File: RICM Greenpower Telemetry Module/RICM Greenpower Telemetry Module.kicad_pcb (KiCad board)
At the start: 2 copper layers, 62.5 x 119 mm, 45 parts, among them J1 Jack-DC, J10 Conn_01x02_Female, J11 Conn_01x02_Female, J2 Conn_01x05_Female, J3 Conn_02x04_Counter_Clockwise, J4 Conn_01x03_Female, J5 Conn_01x03_Female, J6 Conn_01x02_Female, J7 Conn_01x02_Female, J8 Conn_01x02_Female, J9 Conn_01x04_Female, U1 XL2001E1, U2 Pico, U3 MPU_6050_module, U4 Adafruit_MicroSD_SPI_SDIO, U5 ADS7830

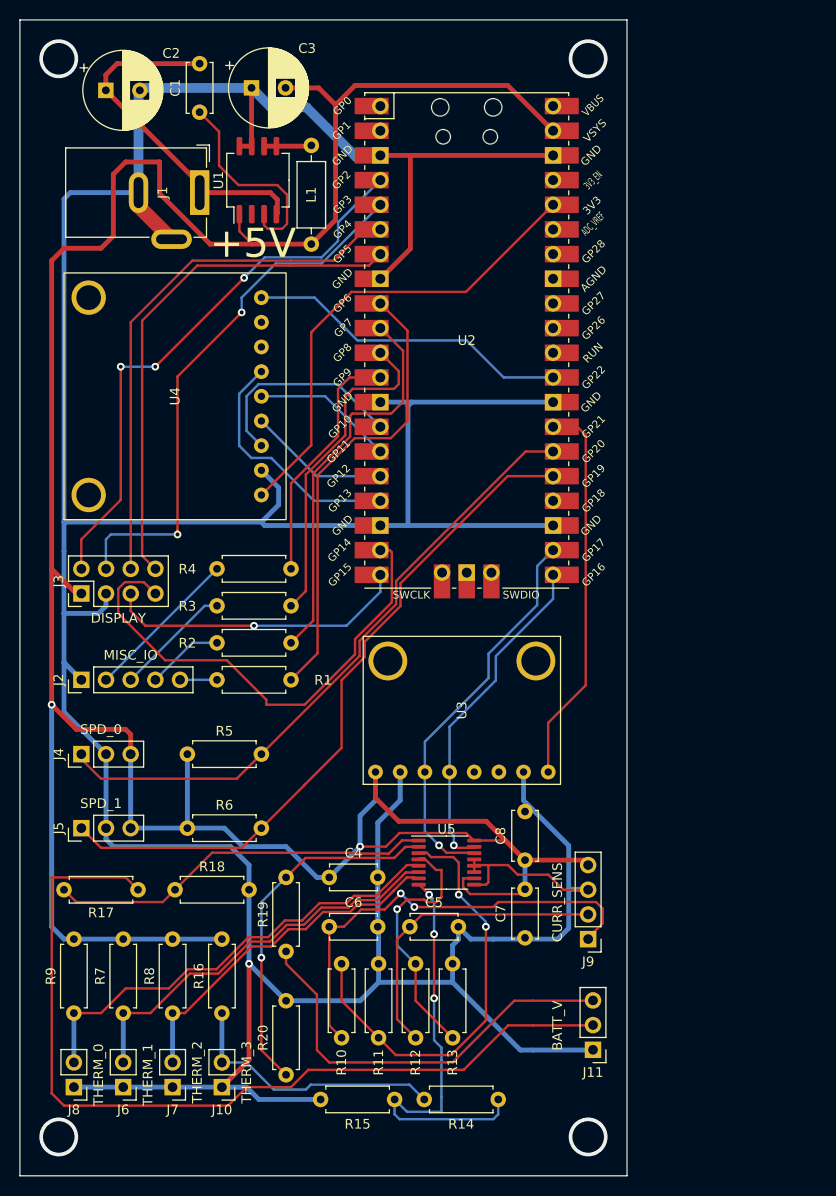
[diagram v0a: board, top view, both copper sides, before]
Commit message: Added pullups for i2c
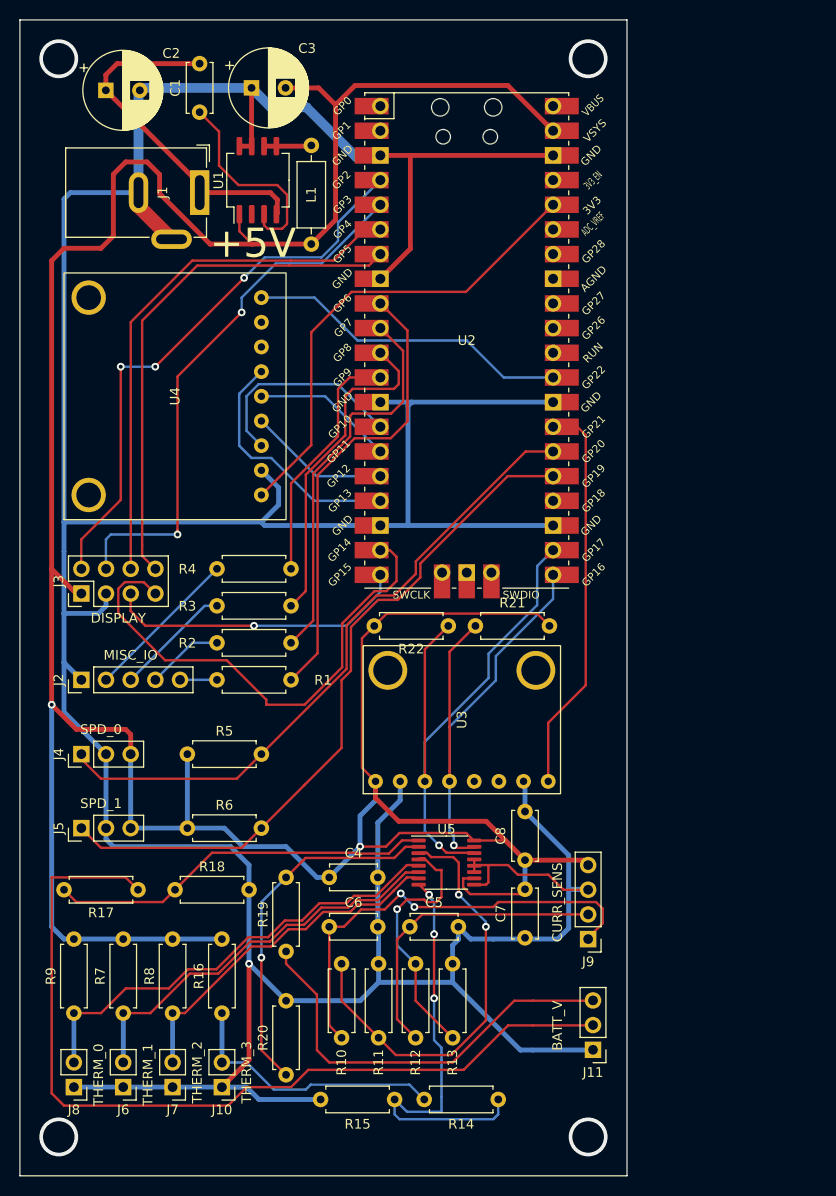
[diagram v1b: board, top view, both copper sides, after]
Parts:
- added R21: 4.7k, Resistor_THT:R_Axial_DIN0207_L6.3mm_D2.5mm_P7.62mm_Horizontal, F.Cu at (56.9, 72.4)
- added R22: 4.7k, Resistor_THT:R_Axial_DIN0207_L6.3mm_D2.5mm_P7.62mm_Horizontal, F.Cu at (54.1, 72.4)
- moved U3 0.96 mm to (55.5, 82.0)
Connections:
- J1 pad 3: GND -> (no net)
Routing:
- net +5V: track 298.1 -> 331.5 mm
- net I2C_SDA: track 34.8 -> 51.9 mm
- net I2C_SCL: track 40.3 -> 57.3 mm
- net GND: track 440.5 -> 438.4 mm
- net SPD_1: track 71.6 -> 72.8 mm
- net I2C0_SDA: track 51.2 -> 52.3 mm
- net SPD_0: track 66.2 -> 67.3 mm
- net ACC_INT: track 37.3 -> 38.3 mm

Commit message: rearranged board
Switched to sdm resistors and capacitors. Added a 3v3 regulated supply. Various other revisions.
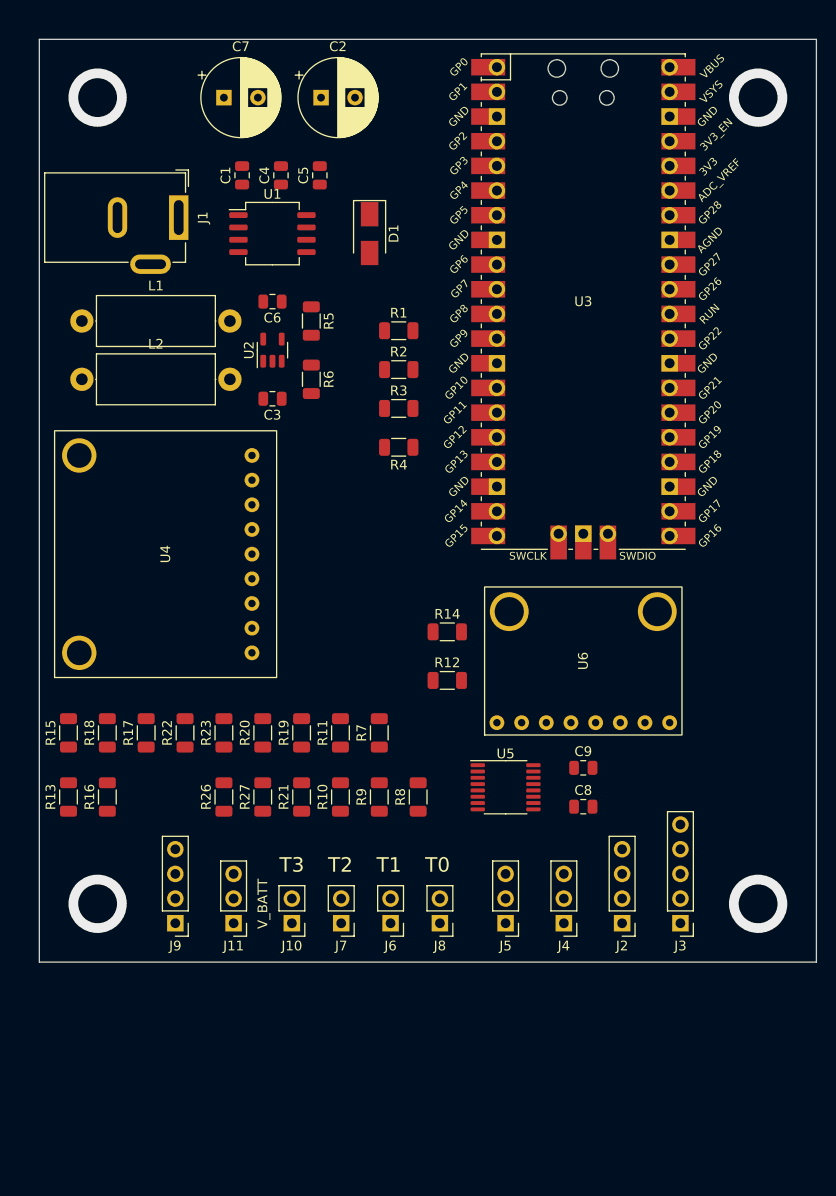
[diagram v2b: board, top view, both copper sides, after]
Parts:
- added C9: 10uf, Capacitor_SMD:C_0805_2012Metric, F.Cu at (68.0, 87.0)
- added D1: D_Schottky, Diode_SMD:D_SMA, F.Cu at (46.0, 32.0)
- added L2: 47uh, Inductor_THT:L_Axial_L12.0mm_D5.0mm_P15.24mm_Horizontal_Fastron_MISC, F.Cu at (16.4, 47.0)
- added R23: 10k, Resistor_SMD:R_1206_3216Metric, F.Cu at (31.0, 83.4)
- added R26: 68k, Resistor_SMD:R_1206_3216Metric, F.Cu at (31.0, 90.0)
- added R27: 10k, Resistor_SMD:R_1206_3216Metric, F.Cu at (35.0, 90.0)
- added U6: MPU_6050_module, Module:MPU_6050_module, F.Cu at (68.0, 76.0)
- C1: value C -> 10uf; footprint Capacitor_THT:C_Disc_D5.0mm_W2.5mm_P5.00mm -> Capacitor_SMD:C_0805_2012Metric
- C2: value C -> 47uf
- C3: value C -> 10uf; footprint Capacitor_THT:CP_Radial_D8.0mm_P3.50mm -> Capacitor_SMD:C_0805_2012Metric
- C4, C6: value 47n -> 10uf; footprint Capacitor_THT:C_Disc_D4.7mm_W2.5mm_P5.00mm -> Capacitor_SMD:C_0805_2012Metric
- C5: value 4.7n -> 10uf; footprint Capacitor_THT:C_Disc_D4.7mm_W2.5mm_P5.00mm -> Capacitor_SMD:C_0805_2012Metric
- C7: value C -> 100uf; footprint Capacitor_THT:C_Disc_D5.0mm_W2.5mm_P5.00mm -> Capacitor_THT:CP_Radial_D8.0mm_P3.50mm
- C8: value C -> 0.1uf; footprint Capacitor_THT:C_Disc_D5.0mm_W2.5mm_P5.00mm -> Capacitor_SMD:C_0805_2012Metric
- J2: value Conn_01x05_Female -> Conn_01x04_Female; footprint Connector_PinHeader_2.54mm:PinHeader_1x05_P2.54mm_Vertical -> Connector_PinHeader_2.54mm:PinHeader_1x04_P2.54mm_Vertical
- J3: value Conn_02x04_Counter_Clockwise -> Conn_01x05_Female; footprint Connector_PinHeader_2.54mm:PinHeader_2x04_P2.54mm_Vertical -> Connector_PinHeader_2.54mm:PinHeader_1x05_P2.54mm_Vertical
- L1: value L -> 47uh; footprint Inductor_THT:L_Axial_L6.6mm_D2.7mm_P10.16mm_Horizontal_Vishay_IM-2 -> Inductor_THT:L_Axial_L12.0mm_D5.0mm_P15.24mm_Horizontal_Fastron_MISC
- R1, R10, R11, R13, R15, R16, R18, R2, R20, R3, R4, R6, R7, R8, R9: footprint Resistor_THT:R_Axial_DIN0207_L6.3mm_D2.5mm_P7.62mm_Horizontal -> Resistor_SMD:R_1206_3216Metric
- R12, R14: value 10k -> 4.7k; footprint Resistor_THT:R_Axial_DIN0207_L6.3mm_D2.5mm_P7.62mm_Horizontal -> Resistor_SMD:R_1206_3216Metric
- R17: value 30k -> 10k; footprint Resistor_THT:R_Axial_DIN0207_L6.3mm_D2.5mm_P7.62mm_Horizontal -> Resistor_SMD:R_1206_3216Metric
- R19: value 68k -> 10k; footprint Resistor_THT:R_Axial_DIN0207_L6.3mm_D2.5mm_P7.62mm_Horizontal -> Resistor_SMD:R_1206_3216Metric
- R21: value 4.7k -> 10k; footprint Resistor_THT:R_Axial_DIN0207_L6.3mm_D2.5mm_P7.62mm_Horizontal -> Resistor_SMD:R_1206_3216Metric
- R22: value 4.7k -> 30k; footprint Resistor_THT:R_Axial_DIN0207_L6.3mm_D2.5mm_P7.62mm_Horizontal -> Resistor_SMD:R_1206_3216Metric
- R5: value 10k -> 47k; footprint Resistor_THT:R_Axial_DIN0207_L6.3mm_D2.5mm_P7.62mm_Horizontal -> Resistor_SMD:R_1206_3216Metric
- U2: value Pico -> MT92165; footprint Module:RPi_Pico_SMD_TH -> Package_TO_SOT_SMD:SOT-23-5
- U3: value MPU_6050_module -> Pico; footprint Module:MPU_6050_module -> Module:RPi_Pico_SMD_TH
- moved C7 87.2 mm to (31.0, 18.0), turned to 0 degrees
- moved C5 77.9 mm to (40.9, 26.0), turned to 90 degrees
- moved C4 72.5 mm to (36.9, 26.0), turned to 90 degrees
- moved J3 70.4 mm to (78.0, 103.0), turned to 180 degrees
- moved C6 64.6 mm to (36.0, 39.0), turned to 180 degrees
- moved J2 61.1 mm to (72.0, 103.0), turned to 180 degrees
- moved J4 52.6 mm to (66.0, 103.0), turned to 180 degrees
- moved R14 48.2 mm to (54.0, 73.0)
- moved R6 47.9 mm to (40.0, 47.0), turned to -90 degrees
- moved R13 46.7 mm to (15.0, 90.0)
- moved R5 46.4 mm to (40.0, 41.0), turned to -90 degrees
- moved R15 45.8 mm to (15.0, 83.4), turned to 90 degrees
- moved U3 44.8 mm to (68.0, 39.0), turned to 0 degrees
- moved J5 44.8 mm to (60.0, 103.0), turned to 180 degrees
- moved J9 42.5 mm to (26.0, 103.0)
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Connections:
- C3 pad 1: GND -> +5V
- C3 pad 2: +5V -> Net-(C3-Pad2)
- C4 pad 1: +5V -> Net-(C1-Pad2)
- C5 pad 1: Net-(C5-Pad1) -> +5V
- C6 pad 1: Net-(C6-Pad1) -> +3V3
- C8 pad 1: +5V -> Net-(C8-Pad1)
- J2 pad 1: GND -> +3V3
- J2 pad 2: Net-(J2-Pad2) -> GND
- J2 pad 3: Net-(J2-Pad3) -> I2C0_SCL
- J2 pad 4: Net-(J2-Pad4) -> I2C0_SDA
- J3 pad 1: +5V -> GND
- J3 pad 2: GND -> Net-(J3-Pad2)
- J3 pad 3: I2C0_SCL -> Net-(J3-Pad3)
- J3 pad 4: I2C0_SDA -> Net-(J3-Pad4)
- J4 pad 3: +5V -> +3V3
- J5 pad 3: +5V -> +3V3
- J9 pad 1: Net-(C6-Pad1) -> +5V
- J9 pad 2: Net-(C5-Pad1) -> GND
- J9 pad 3: GND -> Net-(J9-Pad3)
- J9 pad 4: +5V -> Net-(J9-Pad4)
- R1 pad 1: Net-(J2-Pad5) -> Net-(J3-Pad5)
- R10 pad 1: Net-(C6-Pad1) -> THERM_2
- R10 pad 2: Net-(R10-Pad2) -> +3V3
- R11 pad 1: Net-(R10-Pad2) -> THERM_0
- R11 pad 2: GND -> +3V3
- R12 pad 1: Net-(C5-Pad1) -> I2C_SDA
- R12 pad 2: Net-(R12-Pad2) -> +3V3
- R13 pad 1: Net-(R12-Pad2) -> GND
- R13 pad 2: GND -> Net-(J9-Pad3)
- R14 pad 1: Net-(J10-Pad2) -> I2C_SCL
- R14 pad 2: THERM_3 -> +3V3
- R15 pad 1: GND -> Net-(J9-Pad3)
- R15 pad 2: THERM_3 -> Net-(R15-Pad2)
- R16 pad 1: Net-(J10-Pad2) -> Net-(R15-Pad2)
- R16 pad 2: +5V -> GND
- R17 pad 1: Net-(J11-Pad2) -> Net-(J9-Pad4)
- R19 pad 1: Net-(J11-Pad3) -> Net-(J10-Pad2)
- R19 pad 2: Net-(R19-Pad2) -> THERM_3
- R2 pad 1: Net-(J2-Pad4) -> Net-(J3-Pad4)
- R20 pad 1: Net-(R19-Pad2) -> GND
- R20 pad 2: GND -> THERM_3
- R21 pad 1: I2C_SDA -> Net-(J10-Pad2)
- R21 pad 2: +5V -> +3V3
- R22 pad 1: I2C_SCL -> Net-(J11-Pad2)
- R22 pad 2: +5V -> Net-(R22-Pad2)
- R3 pad 1: Net-(J2-Pad3) -> Net-(J3-Pad3)
- R4 pad 1: Net-(J2-Pad2) -> Net-(J3-Pad2)
- R5 pad 1: +5V -> +3V3
- R5 pad 2: SPD_0 -> Net-(R5-Pad2)
- R6 pad 1: +5V -> GND
- R6 pad 2: SPD_1 -> Net-(R5-Pad2)
- R7 pad 1: THERM_1 -> +3V3
- R7 pad 2: +5V -> SPD_0
- R8 pad 1: THERM_2 -> +3V3
- R8 pad 2: +5V -> SPD_1
- R9 pad 1: THERM_0 -> THERM_1
- R9 pad 2: +5V -> +3V3
- U2 pad 1: unconnected-(U2-Pad1) -> +5V
- U2 pad 2: unconnected-(U2-Pad2) -> GND
- U2 pad 3: GND -> Net-(C3-Pad2)
- U2 pad 4: Net-(J3-Pad8) -> Net-(L2-Pad1)
- U2 pad 5: Net-(J3-Pad7) -> Net-(R5-Pad2)
- U3 pad 1: +5V -> unconnected-(U3-Pad1)
- U3 pad 2: GND -> unconnected-(U3-Pad2)
- U3 pad 3: I2C_SCL -> GND
- U3 pad 4: I2C_SDA -> unconnected-(U3-Pad4)
- U3 pad 7: GND -> unconnected-(U3-Pad7)
- U3 pad 8: ACC_INT -> GND
- U5 pad 1: Net-(R17-Pad2) -> Net-(R22-Pad2)
- U5 pad 10: +5V -> Net-(C8-Pad1)
- U5 pad 16: +5V -> +3V3
- U5 pad 2: Net-(R19-Pad2) -> Net-(R26-Pad2)
- U5 pad 3: Net-(R10-Pad2) -> Net-(R15-Pad2)
- U5 pad 4: Net-(R12-Pad2) -> Net-(R17-Pad2)
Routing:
- net GND: track 438.4 -> 0.00 mm, vias 1 -> 0
- net +5V: track 331.5 -> 0.00 mm, vias 2 -> 0
- net Net-(J11-Pad2): track 91.3 -> 0.00 mm
- net SPD_1: track 72.8 -> 0.00 mm
- net SPD_0: track 67.3 -> 0.00 mm
- net Net-(J3-Pad8): track 58.3 -> 0.00 mm, vias 3 -> 0
- net I2C_SCL: track 57.3 -> 0.00 mm, vias 1 -> 0
- net Net-(J3-Pad7): track 56.0 -> 0.00 mm, vias 2 -> 0
- net Net-(J3-Pad6): track 54.8 -> 0.00 mm
- net Net-(J3-Pad5): track 53.5 -> 0.00 mm
- net I2C0_SDA: track 52.3 -> 0.00 mm
- net I2C_SDA: track 51.9 -> 0.00 mm, vias 1 -> 0
- net +3V3: track 49.2 -> 0.00 mm
- net Net-(R1-Pad2): track 47.1 -> 0.00 mm
- net THERM_0: track 47.0 -> 0.00 mm
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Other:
- board size 62.5 x 119 mm -> 80 x 95 mm
- board text added: "T0"
- board text added: "T1"
- board text added: "T2"
- board text added: "T3"
- board text added: "V_BATT"
- board text removed: "+5V"
- board text removed: "BATT_V"
- board text removed: "CURR_SENS"
- board text removed: "DISPLAY"
- board text removed: "MISC_IO"
- board text removed: "SPD_0"
- board text removed: "SPD_1"
- board text removed: "THERM_0"
- board text removed: "THERM_1"
- board text removed: "THERM_2"
- board text removed: "THERM_3"

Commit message: Moving to laptop
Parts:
- added R5: 10k, Resistor_SMD:R_1206_3216Metric, F.Cu at (86.5, 44.0)
- added R6: 10k, Resistor_SMD:R_1206_3216Metric, F.Cu at (86.5, 49.0)
- R1, R2: value 10k -> 4.7k
- moved R3 40.7 mm to (86.5, 34.0)
- moved R4 40.4 mm to (86.5, 39.0), turned to 0 degrees
- moved C2 25.8 mm to (18.0, 29.7), turned to 90 degrees
- moved R2 20.1 mm to (51.0, 66.0), turned to 180 degrees
- moved R1 19.1 mm to (51.0, 61.0), turned to 180 degrees
- moved J1 17.6 mm to (43.6, 27.4), turned to 180 degrees
- moved C1 8.12 mm to (25.0, 24.0)
- moved C4 8.12 mm to (29.0, 24.0)
- moved C5 8.12 mm to (33.0, 24.0)
- moved U1 6.00 mm to (30.0, 32.0)
- moved C7 3.07 mm to (28.0, 18.7), turned to 90 degrees
- moved D1 2.83 mm to (44.0, 34.0), turned to 0 degrees
- moved L1 1.38 mm to (15.0, 41.0)
- moved L2 1.38 mm to (15.0, 47.0)
- moved R7 1.00 mm to (41.0, 41.0)
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- renumbered R8 to R10, R9 to R11, R10 to R12, R11 to R13, R12 to R14, R13 to R15, R14 to R16, R15 to R17, R16 to R18, R17 to R19, R18 to R20, R19 to R21, R20 to R22, R21 to R23, R22 to R24, R23 to R25, R5 to R7, R6 to R8, R7 to R9
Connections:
- D1 pad 1: GND -> Net-(L1-Pad1)
- D1 pad 2: Net-(D1-Pad2) -> GND
- L1 pad 1: Net-(D1-Pad2) -> Net-(L1-Pad1)
- R1 pad 1: Net-(J3-Pad5) -> I2C0_SDA
- R1 pad 2: Net-(R1-Pad2) -> +3V3
- R2 pad 1: Net-(J3-Pad4) -> I2C0_SCL
- R2 pad 2: Net-(R2-Pad2) -> +3V3
- R3 pad 1: Net-(J3-Pad3) -> Net-(R3-Pad1)
- R3 pad 2: Net-(R3-Pad2) -> Net-(J3-Pad5)
- R4 pad 1: Net-(J3-Pad2) -> Net-(R4-Pad1)
- R4 pad 2: Net-(R4-Pad2) -> Net-(J3-Pad4)
- U1 pad 5: Net-(D1-Pad2) -> Net-(L1-Pad1)
- U1 pad 6: Net-(D1-Pad2) -> Net-(L1-Pad1)
- U3 pad 10: Net-(R2-Pad2) -> Net-(R4-Pad1)
- U3 pad 11: Net-(R3-Pad2) -> Net-(R5-Pad1)
- U3 pad 12: Net-(R4-Pad2) -> Net-(R6-Pad1)
- U3 pad 9: Net-(R1-Pad2) -> Net-(R3-Pad1)
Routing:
- net GND: track 0.00 -> 435.0 mm, vias 0 -> 5
- net +5V: track 0.00 -> 175.9 mm, vias 0 -> 3
- net +3V3: track 0.00 -> 174.2 mm, vias 0 -> 7
- net SPD_0: track 0.00 -> 79.8 mm, vias 0 -> 2
- net SPD_1: track 0.00 -> 74.9 mm, vias 0 -> 5
- net Net-(J3-Pad5): track 0.00 -> 63.8 mm, vias 0 -> 2
- net Net-(J3-Pad4): track 0.00 -> 61.3 mm, vias 0 -> 2
- net Net-(J3-Pad3): track 0.00 -> 58.0 mm
- net I2C0_SDA: track 0.00 -> 57.7 mm, vias 0 -> 3
- net SD_DET: track 0.00 -> 57.7 mm, vias 0 -> 2
- net I2C0_SCL: track 0.00 -> 56.9 mm, vias 0 -> 2
- net Net-(J3-Pad2): track 0.00 -> 55.6 mm
- net I2C_SCL: track 0.00 -> 55.0 mm, vias 0 -> 2
- net Net-(C1-Pad2): track 0.00 -> 53.6 mm, vias 0 -> 1
- net I2C_SDA: track 0.00 -> 52.9 mm, vias 0 -> 1
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
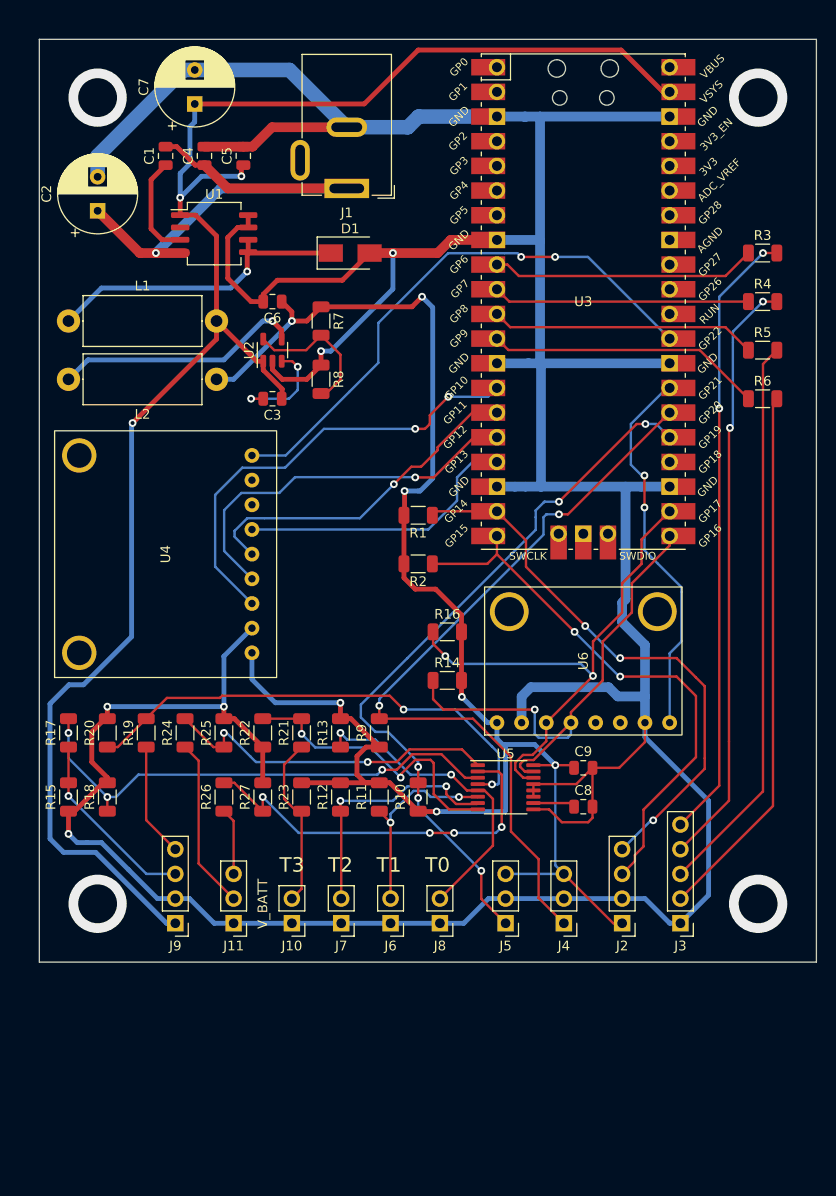
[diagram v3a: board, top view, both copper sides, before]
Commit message: fixed errors discovered in v1 board
Connected vref on the ADS7830 to 3v3.
Corrected swapped pins on MT9216.
Added silkscreens and readjusted connector numbering.
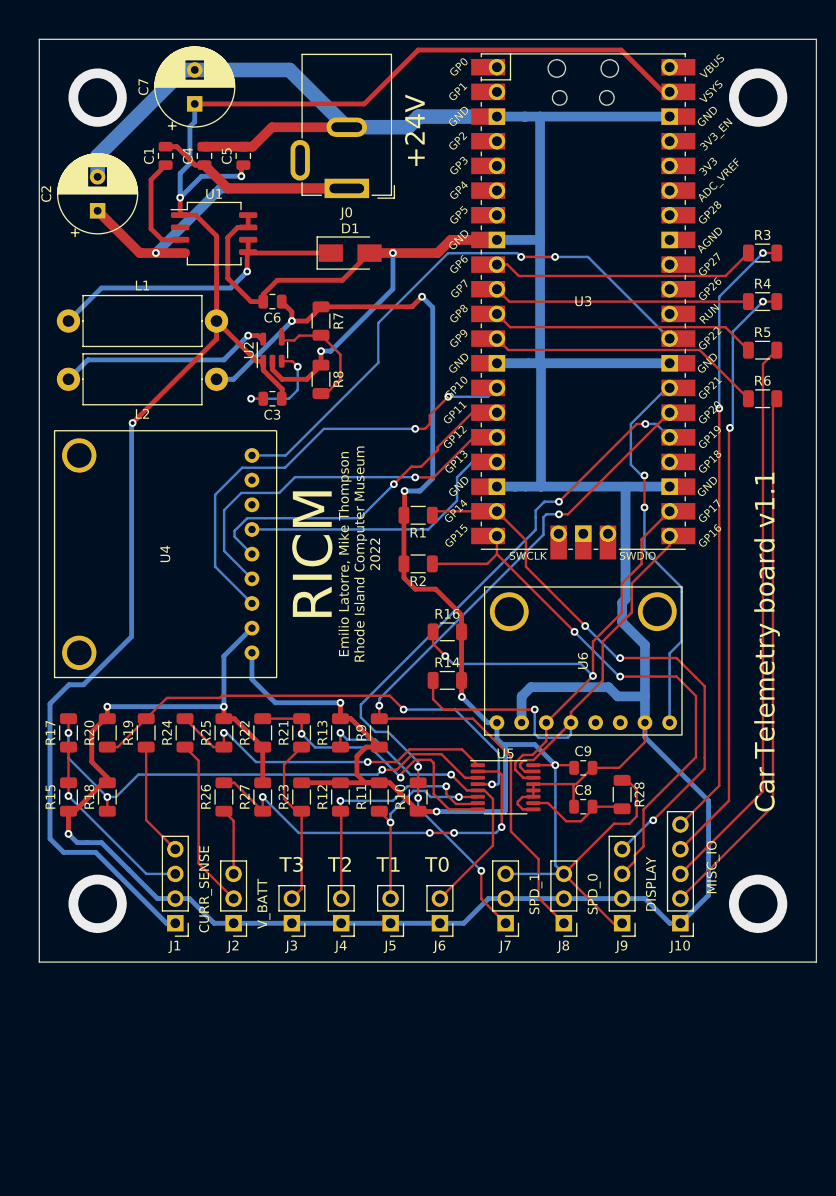
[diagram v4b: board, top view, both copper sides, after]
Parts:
- added R28: 10k, Resistor_SMD:R_1206_3216Metric, F.Cu at (72.0, 89.8)
- renumbered J1 to J0, J9 to J1, J3 to J10, J11 to J2, J10 to J3, J7 to J4, J6 to J5, J8 to J6, J5 to J7, J4 to J8, J2 to J9
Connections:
- C8 pad 1: Net-(C8-Pad1) -> GND
- C8 pad 2: GND -> Net-(U5-Pad10)
- U2 pad 4: Net-(L2-Pad1) -> Net-(R7-Pad2)
- U2 pad 5: Net-(R7-Pad2) -> Net-(L2-Pad1)
- U5 pad 10: Net-(C8-Pad1) -> Net-(U5-Pad10)
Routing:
- net +3V3: track 174.2 -> 188.8 mm
- net Net-(U5-Pad10): track 0.00 -> 11.1 mm
- net GND: track 435.0 -> 429.7 mm
- net Net-(C8-Pad1): track 4.34 -> 0.00 mm
- net Net-(L2-Pad1): track 25.7 -> 22.1 mm
- net Net-(R7-Pad2): track 15.0 -> 13.1 mm
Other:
- board text added: "+24V"
- board text added: "CURR_SENSE"
- board text added: "Car Telemetry board v1.1"
- board text added: "DISPLAY"
- board text added: "Emilio Latorre, Mike Thompson Rhode Island Computer Museum 2022"
- board text added: "MISC_IO"
- board text added: "RICM"
- board text added: "SPD_0"
- board text added: "SPD_1"

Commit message: Fixed footprints and silkscreen
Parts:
- C2: footprint Capacitor_THT:CP_Radial_D8.0mm_P3.50mm -> Capacitor_THT:CP_Radial_D5.0mm_P2.00mm
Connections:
- net I2C0_SCL renamed I2C1_SCL
- net I2C0_SDA renamed I2C1_SDA
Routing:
- net GND: track 429.7 -> 430.7 mm
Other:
- board text added: "R21,22,23 Optional For T3"
